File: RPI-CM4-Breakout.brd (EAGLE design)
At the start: 70 x 59 mm, 26 parts, among them IC1 MC74VHC1G14DFT1G, J1 P1-100, J2 P101-200, J3 47571-0001

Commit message: Added USB block
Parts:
- removed JP1: JUMPER-SMT_2_NC_TRACE_NO-SILK, SparkFun-Jumpers:SMT-JUMPER_2_NC_TRACE_NO-SILK
- removed TP2: TEST-POINT3X5, SparkFun-Connectors:PAD.03X.05
- added C10, C11, C12, C13, C14, C9: 10uF, rcl:C0805
- added C15, C16, C17, C18, C19: 100nF, rcl:C0603
- added C5, C6: 27pF, rcl:C0603
- added C7: (no value), rcl:C0805
- added C8: 100uF, SparkFun-Capacitors:EIA7343
- added R10, R9: 12K, rcl:R0603
- added R11: 2K2, rcl:R0603
- added R12: 15K, rcl:R0603
- added R5, R6, R7, R8: 36K, rcl:R0603
- added TP8, TP9: TEST-POINT3X5, SparkFun-Connectors:PAD.03X.05
- added U1: USB2514B-I/M2, USB2514B-I_M2:QFN50P600X600X100-37N
- added U2: FSUSB42MUX, FSUSB42MUX:SOP50P490X110-10N
- added U3: AP22653W6-7, AP22653W6-7:SOT95P280X145-6N
- added U4: TPD4EUSB30DQAR, TPD4EUSB30DQAR:IC_TPD4EUSB30DQAR
- added Y1: 24MHz, crystal:SM49
- J4: device SparkFun-Connectors:1X04_SMD_RA_FEMALE -> EAGLE-INPUT_OUTPUT_CONNECTORS-rev17a:629104190121
- J5: value (none) -> 72309-8034BLF; device EAGLE-INPUT_OUTPUT_CONNECTORS-rev17a:629104190121 -> 72309-8034BLF:FRAMATOME_72309-8034BLF
- R2, R3: value 5.1k -> (none)
- moved J5 144.7 mm to (-11.4, -116.8), turned to 0 degrees
- moved J4 59.2 mm to (17.9, 24.9), turned to 270 degrees
- renumbered CN1 to HDMI1
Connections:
- net N$10 renamed PCIE_NRST
- net N$100 renamed HDMI1_D0_P
- net N$102 renamed HDMI1_D0_N
- net N$106 renamed HDMI1_CK_P
- net N$108 renamed HDMI1_CK_N
- net N$11 renamed PCIE_CLK_P
- net N$129 renamed DSI1_C_N
- net N$13 renamed PCIE_CLK_N
- net N$131 renamed DSI1_C_P
- net N$135 renamed DSI1_D2_N
- net N$136 renamed DSI1_D3_N
- net N$137 renamed DSI1_D2_P
- net N$138 renamed DSI1_D3_P
- net N$20 renamed PCIE_RX_P
- net N$22 renamed PCIE_RX_N
- net N$25 renamed GPIO21
- net N$26 renamed GPIO19
- net N$27 renamed GPIO20
- net N$28 renamed GPIO13
- net N$29 renamed GPIO16
- net N$3 renamed PCIE_CLK_NREQ
- net N$30 renamed GPIO6
- net N$31 renamed GPIO12
- net N$33 renamed PCIE_TX_P
- net N$34 renamed GPIO5
- net N$35 renamed ID_SC
- net N$36 renamed ID_SD
- net N$37 renamed GPIO7
- net N$38 renamed GPIO11
- net N$39 renamed GPIO8
- net N$40 renamed GPIO9
- net N$41 renamed GPIO25
- net N$43 renamed PCIE_TX_N
- net N$44 renamed GPIO10
- net N$45 renamed GPIO24
- net N$46 renamed GPIO22
- net N$47 renamed GPIO23
- net N$48 renamed GPIO27
- net N$49 renamed GPIO18
- net N$50 renamed GPIO17
- net N$54 renamed GPIO4
- net N$56 renamed GPIO3
- net N$58 renamed CAM0_D0_N
- net N$60 renamed CAM0_D0_P
- net N$65 renamed CAM0_D1_N
- net N$67 renamed CAM0_D1_P
- net N$75 renamed CAM0_C_N
- net N$77 renamed CAM0_C_P
- net N$78 renamed HDMI1_HOTPLUG
- net N$80 renamed SCL0
- net N$81 renamed HDMI1_SDA
- net N$82 renamed SDA0
- net N$83 renamed HDMI1_D2_P
- net N$84 renamed HDMI1_SCL
- net N$85 renamed HDMI1_D2_N
- net N$86 renamed HDMI1_CEC
- net N$89 renamed WL_NDIS
- net N$90 renamed HDMI1_D1_P
- net N$91 renamed BT_NDIS
- net N$93 renamed HDMI1_D1_N
- removed net USBOTG_ID: J2.1, TP5.P$1
- new net HD1_N: J5.A2, U1.1
- new net HD1_P: J5.A3, U1.2
- new net HD2_N: J5.B2, U1.3
- new net HD2_P: J5.B3, U1.4
- new net N$10: R8.2, U1.24
- new net N$11: R9.1, U1.35
- new net N$13: C5.1, U1.33, Y1.1
- new net N$14: C6.1, U1.32, Y1.2
- new net N$15: R10.1, R11.2, U2.2
- new net N$20: R12.2, U3.5
- new net N$3: R5.2, U1.25
- new net N$8: R6.2, U1.28
- new net N$9: R7.2, U1.22
- new net NOCS1: U1.13, U1.17, U1.19, U1.21, U3.4
- new net PWR1: U1.12, U3.3
- new net USBD_N: J4.3, U2.8, U4.4, U4.7
- new net USBD_P: J4.2, U2.9, U4.5, U4.6
- new net USBH_N: U1.30, U2.6
- new net USBH_P: U1.31, U2.7
- new net USBOTG: J2.1, J4.1, R11.1, TP5.P$1
- new net VBUS: C10.1, C11.1, C12.1, C8.A, C9.1, J5.A1, J5.B1, U3.6
- net 3.3V: now also C13.1, C14.1, C15.1, C16.1, C17.1, C18.1, C19.1, U1.10, U1.15, U1.23, U1.27, U1.29, U1.36, U1.5, U2.1; no longer J4.1, JP1.1
- net 5.0V: now also C7.1, U3.1; no longer J5.1
- net GND: now also C10.2, C11.2, C12.2, C13.2, C14.2, C15.2, C16.2, C17.2, C18.2, C19.2, C5.2, C6.2, C7.2, C8.C, C9.2, J4.SHELL, J4.SHELL1, J4.SHELL2, J4.SHELL3, J5.1, J5.2, J5.A4, J5.B4, R10.2, R12.1, R5.1, R6.1, R7.1, R8.1, R9.2, U1.37, U2.10, U2.5, U3.2, U4.3, U4.8; no longer J5.4, J5.SHELL, J5.SHELL1, J5.SHELL2, J5.SHELL3
- net GPIO14: no longer J4.3
- net GPIO15: no longer J4.2
- net GPIO_VREF: no longer JP1.2
- net N$6: now also TP8.P$1
- net N_EXTRST: now also TP9.P$1, U1.26; no longer TP2.P$1
- net USB2_N: now also U2.4; no longer J5.2
- net USB2_P: now also U2.3; no longer J5.3
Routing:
- net 3.3V: track 118.7 -> 70.8 mm
- net GPIO_VREF: track 5.26 -> 41.4 mm
- net USB2_P: track 20.0 -> 0.00 mm
- net USB2_N: track 18.6 -> 0.00 mm
- net N_PWR_LED: track 13.5 -> 0.00 mm
- net N_EXTRST: track 6.29 -> 1.03 mm
- net USBOTG_ID: track 4.13 -> 0.00 mm
- net USBOTG: track 0.00 -> 4.13 mm
- net N$6: track 2.24 -> 4.26 mm
- net 5.0V: track 139.5 -> 138.8 mm
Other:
- board text added: "HDMI"
- board text added: "SD CARD"
- board text added: "USB-A"
- board text added: "USB-C"

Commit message: Initial layout
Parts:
- removed C1: 10uF, SparkFun-Capacitors:0603
- removed HDMI1: (no value), microbuilder:HDMI_MOLEX_47151-0001
- removed J3: 47571-0001, SamacSys_Parts:47571-0001
- removed TP6, TP7: TEST-POINT3X5, SparkFun-Connectors:PAD.03X.05
- added C20: (no value), rcl:C0603
- added C21: 10uF, SparkFun-Capacitors:0603
- added HDMI2: (no value), microbuilder:HDMI_MOLEX_47151-0001
- added J6: ARJM11A1-502-JJ-EW2, ARJM11A1-502-JJ-EW2:ABRACON_ARJM11A1-502-JJ-EW2
- added J7: 47571-0001, SamacSys_Parts:47571-0001
- added R13, R14: 470R, rcl:R0603
- added U5, U6: TPD4EUSB30DQAR, TPD4EUSB30DQAR:IC_TPD4EUSB30DQAR
- C7: value (none) -> 10uF
- moved C19 195.2 mm to (66.4, 11.7), flipped to the bottom, turned to 90 degrees
- moved C16 191.5 mm to (58.4, 26.5), flipped to the bottom, turned to 180 degrees
- moved C18 189.5 mm to (63.9, 11.7), flipped to the bottom, turned to 90 degrees
- moved C17 188.1 mm to (60.5, 16.8), flipped to the bottom, turned to 90 degrees
- moved C15 182.1 mm to (69.7, 15.5), flipped to the bottom, turned to 90 degrees
- moved C14 176.8 mm to (70.2, 15.5), turned to 90 degrees
- moved C13 168.0 mm to (60.3, 17.3), turned to 90 degrees
- moved J5 159.3 mm to (86.4, 8.89), turned to 90 degrees
- moved U4 153.6 mm to (63.5, 24.1), turned to 180 degrees
- moved C12 149.5 mm to (87.6, 5.46), flipped to the bottom, turned to 180 degrees
- moved C11 146.3 mm to (72.3, 20.1), flipped to the bottom, turned to 180 degrees
- moved C10 143.6 mm to (72.3, 23.1), flipped to the bottom, turned to 180 degrees
- moved C9 137.5 mm to (87.6, 7.62), flipped to the bottom, turned to 180 degrees
- moved C8 129.8 mm to (72.3, 21.6), turned to 180 degrees
- moved C7 119.8 mm to (65.0, 22.6), flipped to the bottom
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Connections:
- new net CT: C20.1, J6.5, J6.6
- new net GND_3: U5.3, U5.8, U6.3, U6.8
- new net N$22: J6.L2, R13.1
- new net N$23: J6.L3, R14.2
- net 3.3V: now also C21.1, J6.L1, J6.L4, J7.P4; no longer C1.1, J3.P4
- net 5.0V: now also HDMI2.18; no longer HDMI1.18
- net ETH_LEDG: now also R13.2
- net ETH_LEDY: now also R14.1
- net GND: now also C20.2, C21.2, HDMI2.11, HDMI2.17, HDMI2.2, HDMI2.5, HDMI2.8, HDMI2.P$1, HDMI2.P$2, HDMI2.P$3, HDMI2.P$4, J7.G1, J7.G2, J7.G3, J7.P6; no longer C1.2, HDMI1.11, HDMI1.17, HDMI1.2, HDMI1.5, HDMI1.8, HDMI1.P$1, HDMI1.P$2, HDMI1.P$3, HDMI1.P$4, J3.G1, J3.G2, J3.G3, J3.P6
- net GPIO14: no longer TP7.P$1
- net GPIO15: no longer TP6.P$1
- net HDMI0_CK_N: now also HDMI2.12; no longer HDMI1.12
- net HDMI0_CK_P: now also HDMI2.10; no longer HDMI1.10
- net HDMI0_D0_N: now also HDMI2.9; no longer HDMI1.9
- net HDMI0_D0_P: now also HDMI2.7; no longer HDMI1.7
- net HDMI0_D1_N: now also HDMI2.6; no longer HDMI1.6
- net HDMI0_D1_P: now also HDMI2.4; no longer HDMI1.4
- net HDMI0_D2_N: now also HDMI2.3; no longer HDMI1.3
- net HDMI0_D2_P: now also HDMI2.1; no longer HDMI1.1
- net HDMI0_HOTPLUG: now also HDMI2.19; no longer HDMI1.19
- net HDMI0_SCL: now also HDMI2.15; no longer HDMI1.15
- net HDMI0_SDA: now also HDMI2.16; no longer HDMI1.16
- net NOCS1: no longer U1.19, U1.21
- net SD_CLK: now also J7.P5; no longer J3.P5
- net SD_CMD: now also J7.P3; no longer J3.P3
- net SD_DAT0: now also J7.P7; no longer J3.P7
- net SD_DAT1: now also J7.P8; no longer J3.P8
- net SD_DAT2: now also J7.P1; no longer J3.P1
- net SD_DAT3: now also J7.P2; no longer J3.P2
- net TRD0_N: now also J6.2, U6.2, U6.9
- net TRD0_P: now also J6.1, U6.1, U6.10
- net TRD1_N: now also J6.4, U6.4, U6.7
- net TRD1_P: now also J6.3, U6.5, U6.6
- net TRD2_N: now also J6.8, U5.2, U5.9
- net TRD2_P: now also J6.7, U5.1, U5.10
- net TRD3_N: now also J6.10, U5.4, U5.7
- net TRD3_P: now also J6.9, U5.5, U5.6
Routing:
- net 5.0V: track 138.8 -> 18.4 mm, vias 0 -> 2
- net GND: track 84.1 -> 0.00 mm, vias 0 -> 5
- net 3.3V: track 70.8 -> 4.04 mm
- net GPIO_VREF: track 41.4 -> 0.00 mm
- net SD_CMD: track 40.0 -> 0.00 mm
- net N_PWR_LED: track 0.00 -> 30.0 mm
- net SD_DAT1: track 27.2 -> 0.00 mm
- net SD_DAT0: track 24.7 -> 0.00 mm
- net VBUS: track 0.00 -> 22.3 mm, vias 0 -> 2
- net RUN_PG: track 18.4 -> 0.00 mm
- net SD_CLK: track 17.8 -> 0.00 mm
- net SD_DAT2: track 13.0 -> 0.00 mm
- net SD_DAT3: track 12.8 -> 0.00 mm
- net A0/CC2: track 8.88 -> 2.25 mm
- net GPIO14: track 6.50 -> 0.00 mm
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- removed copper zone on layer 1, net GND
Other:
- board size 70 x 59 mm -> 95.5 x 59.1 mm
- board text removed: "SD CARD"

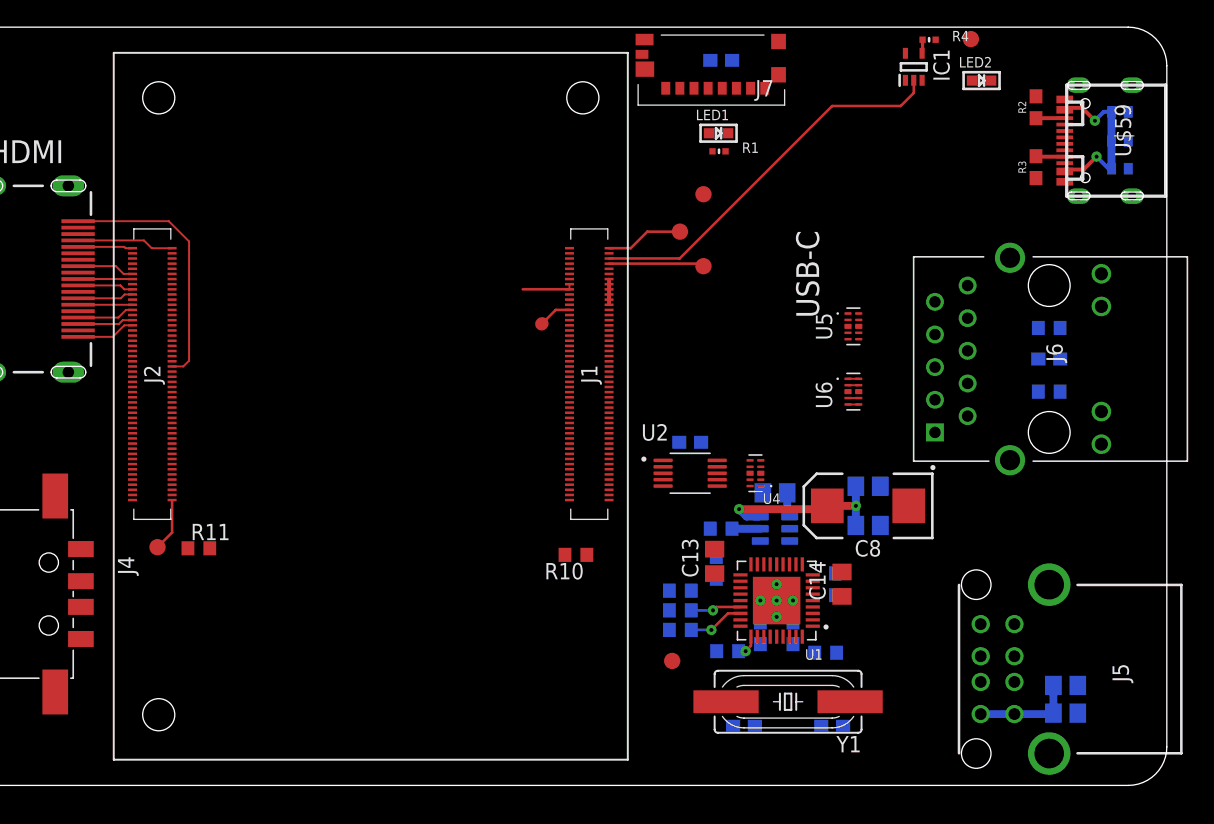
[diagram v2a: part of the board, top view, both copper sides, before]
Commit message: Moved CM4 to bottom side
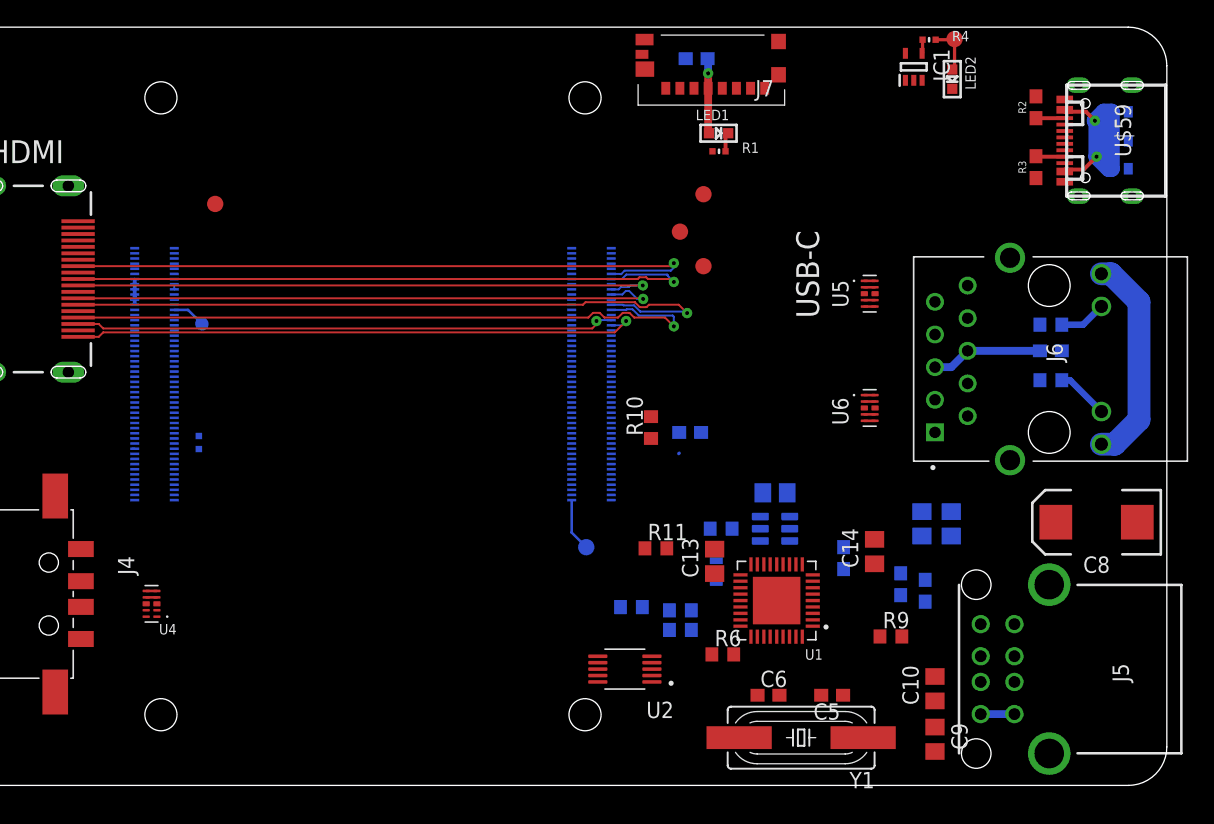
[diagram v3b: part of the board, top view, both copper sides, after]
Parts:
- added R15: 0R, microbuilder:_0402MP
- moved TP9 50.3 mm to (21.5, 45.1)
- moved U4 48.1 mm to (16.5, 14.0)
- moved R11 35.6 mm to (55.8, 18.3)
- moved J2 34.2 mm to (50.7, 31.8), flipped to the bottom
- moved J1 33.8 mm to (16.7, 31.8), flipped to the bottom
- moved TP5 33.4 mm to (50.3, 18.4), flipped to the bottom
- moved C8 17.8 mm to (90.0, 20.3)
- moved C12 17.2 mm to (78.7, 20.2), turned to 90 degrees
- moved C10 16.6 mm to (77.5, 7.37), flipped to the top, turned to 90 degrees
- moved U2 16.1 mm to (53.3, 8.89), turned to 180 degrees
- moved C18 13.2 mm to (76.7, 15.0), turned to 270 degrees
- moved R10 11.5 mm to (55.4, 27.7), turned to 90 degrees
- moved C9 11.0 mm to (77.5, 3.43), flipped to the top, turned to 270 degrees
- moved C19 7.04 mm to (70.4, 17.5), turned to 270 degrees
- moved R9 5.24 mm to (74.0, 11.4), flipped to the top, turned to 0 degrees
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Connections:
- net EEPROM_NWP: now also R15.2
- net GND: now also R15.1
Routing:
- net HDMI0_D1_N: track 4.24 -> 54.2 mm, vias 0 -> 1
- net HDMI0_D1_P: track 4.48 -> 53.1 mm, vias 0 -> 1
- net HDMI0_CK_P: track 4.24 -> 51.9 mm, vias 0 -> 1
- net HDMI0_CK_N: track 4.48 -> 51.9 mm, vias 0 -> 1
- net HDMI0_D0_P: track 4.36 -> 46.8 mm, vias 0 -> 1
- net HDMI0_D0_N: track 4.36 -> 46.5 mm, vias 0 -> 1
- net HDMI0_D2_P: track 4.61 -> 44.4 mm, vias 0 -> 1
- net HDMI0_D2_N: track 4.36 -> 42.1 mm, vias 0 -> 1
- net N_PWR_LED: track 30.0 -> 0.00 mm
- net HDMI0_HOTPLUG: track 20.1 -> 0.00 mm
- net VBUS: track 22.3 -> 2.62 mm, vias 2 -> 0
- net 3.3V: track 4.04 -> 23.0 mm, vias 0 -> 1
- net CT: track 0.00 -> 8.69 mm
- net HDMI0_SDA: track 7.56 -> 0.00 mm
- net N_RPIBOOT: track 7.43 -> 0.00 mm
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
